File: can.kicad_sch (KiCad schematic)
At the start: 43 parts, among them Q3 2N7002, U5 TJA1051T/3, U6 MCP2518FD, U7 TJA1051T/3, Y1 40MHz

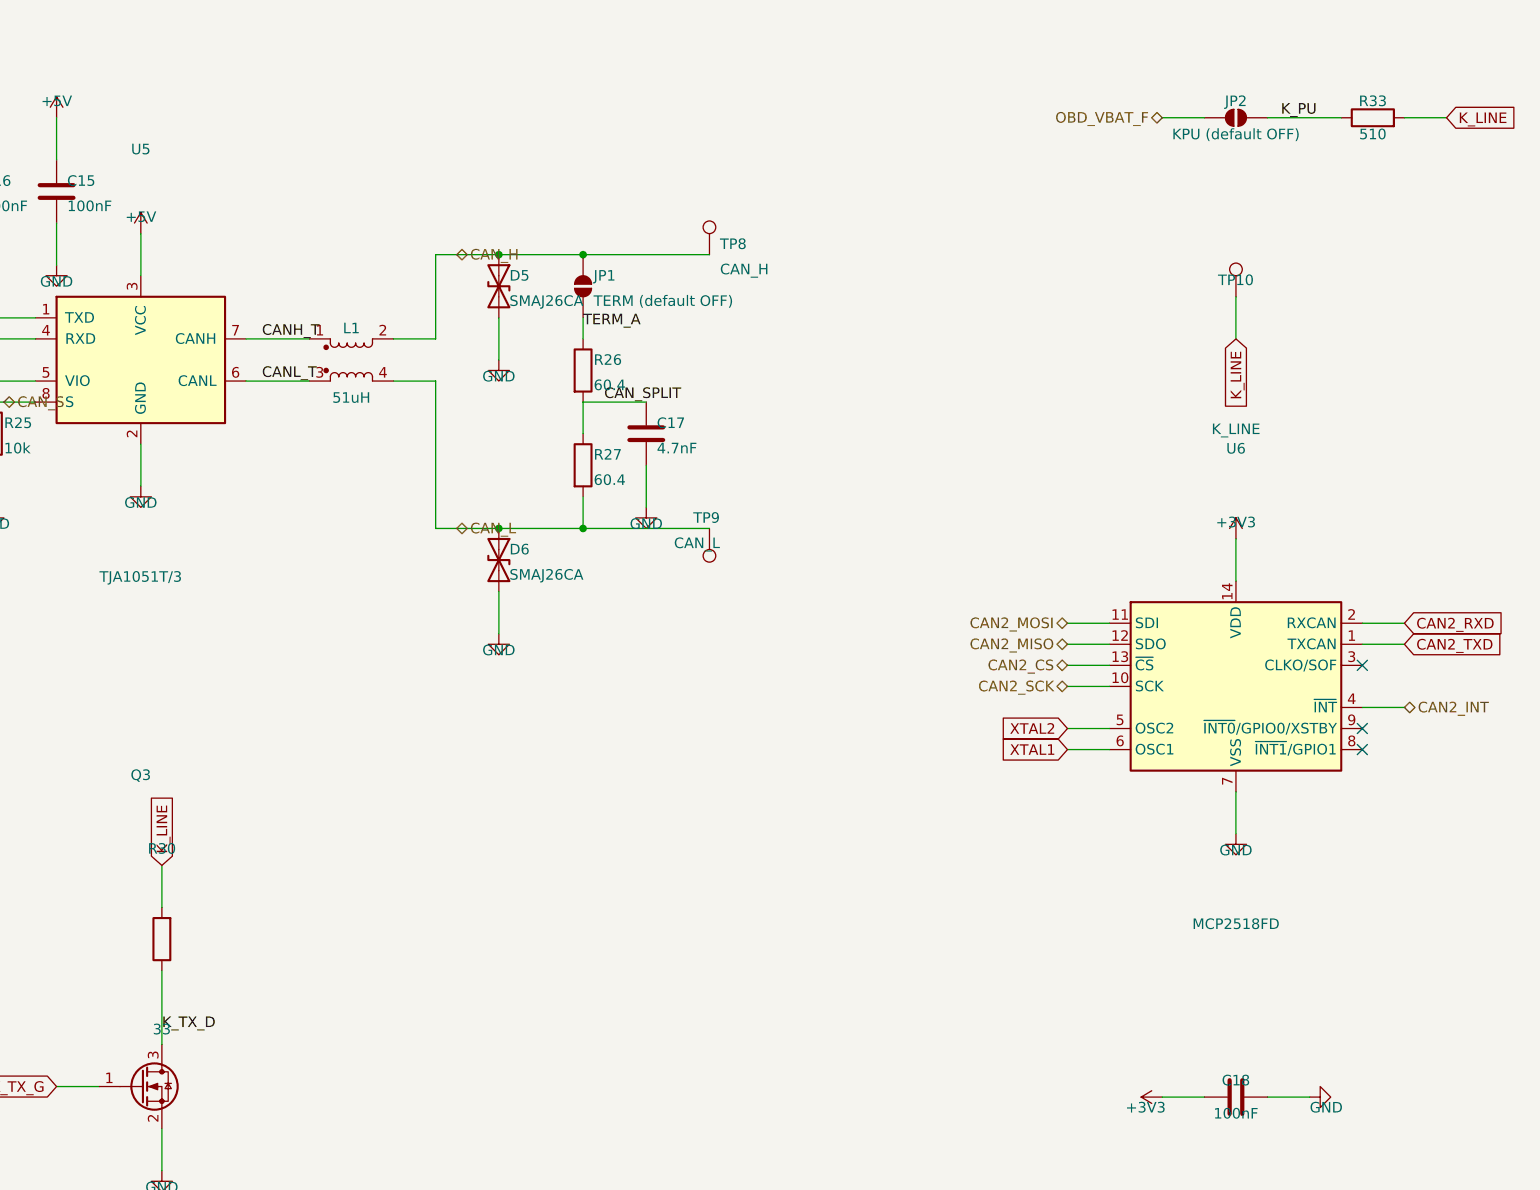
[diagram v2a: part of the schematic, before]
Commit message: Route, audit and document the carrier; verify every part number against the catalogue
Ordering is the point of this pass, so the part numbers came first. Every
LCSC number on the board was opened and read -- manufacturer part, package,
and the parameter that decides whether it is the right part. That found:

  C2148396 for the MCP2518FD    is an 18.7k resistor, out of stock -> C626759
  C255909  for a 40 MHz crystal is a 16 MHz crystal              -> C5186937
  C157966  for a JST PH 10-way  is a JST XH 9-way, 2.5 mm pitch  -> C158038

Three of the five numbers introduced last sitting were wrong, and all three
were plausible enough that the BOM exported clean. docs/PARTS.md records the
lot, including that LCSC's own listing for the microSD socket claims it has
no card-detect switch -- it has one, and the schematic is right.

Two footprints would not have soldered: both polyfuses are 1812 parts sitting
on a 1206 land, inherited from the parent board where nothing had ever
compared a part's package against its footprint. And the generic-passive
table was keyed on value alone, so the 1206 positions added last sitting
would have ordered 0805 parts -- right resistance, wrong footprint, every
board. It is keyed on (value, package) now and returns nothing rather than
guessing, so an unmatched line has no part number and somebody has to look.

Several values moved to match what is actually stocked: the power-fail
divider to 43k/18k (same trip point to 2 mV, both stocked 1 % parts), the
K-line series and pull-up to 20 R and 750 R, and the supercap charge resistor
from 22 R to 100 R -- 22 R put 1 W into a 250 mW part for the first several
seconds of every power-up.

Two real defects, both found by tools rather than by reading:

  - The hold-up Schottky was BACKWARDS. Reversed it shorts out the inrush
    limiter and blocks the discharge, so the supercap bank could never hold
    the rail up and the whole hold-up circuit was inert. audit_polarity found
    it once its expectat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
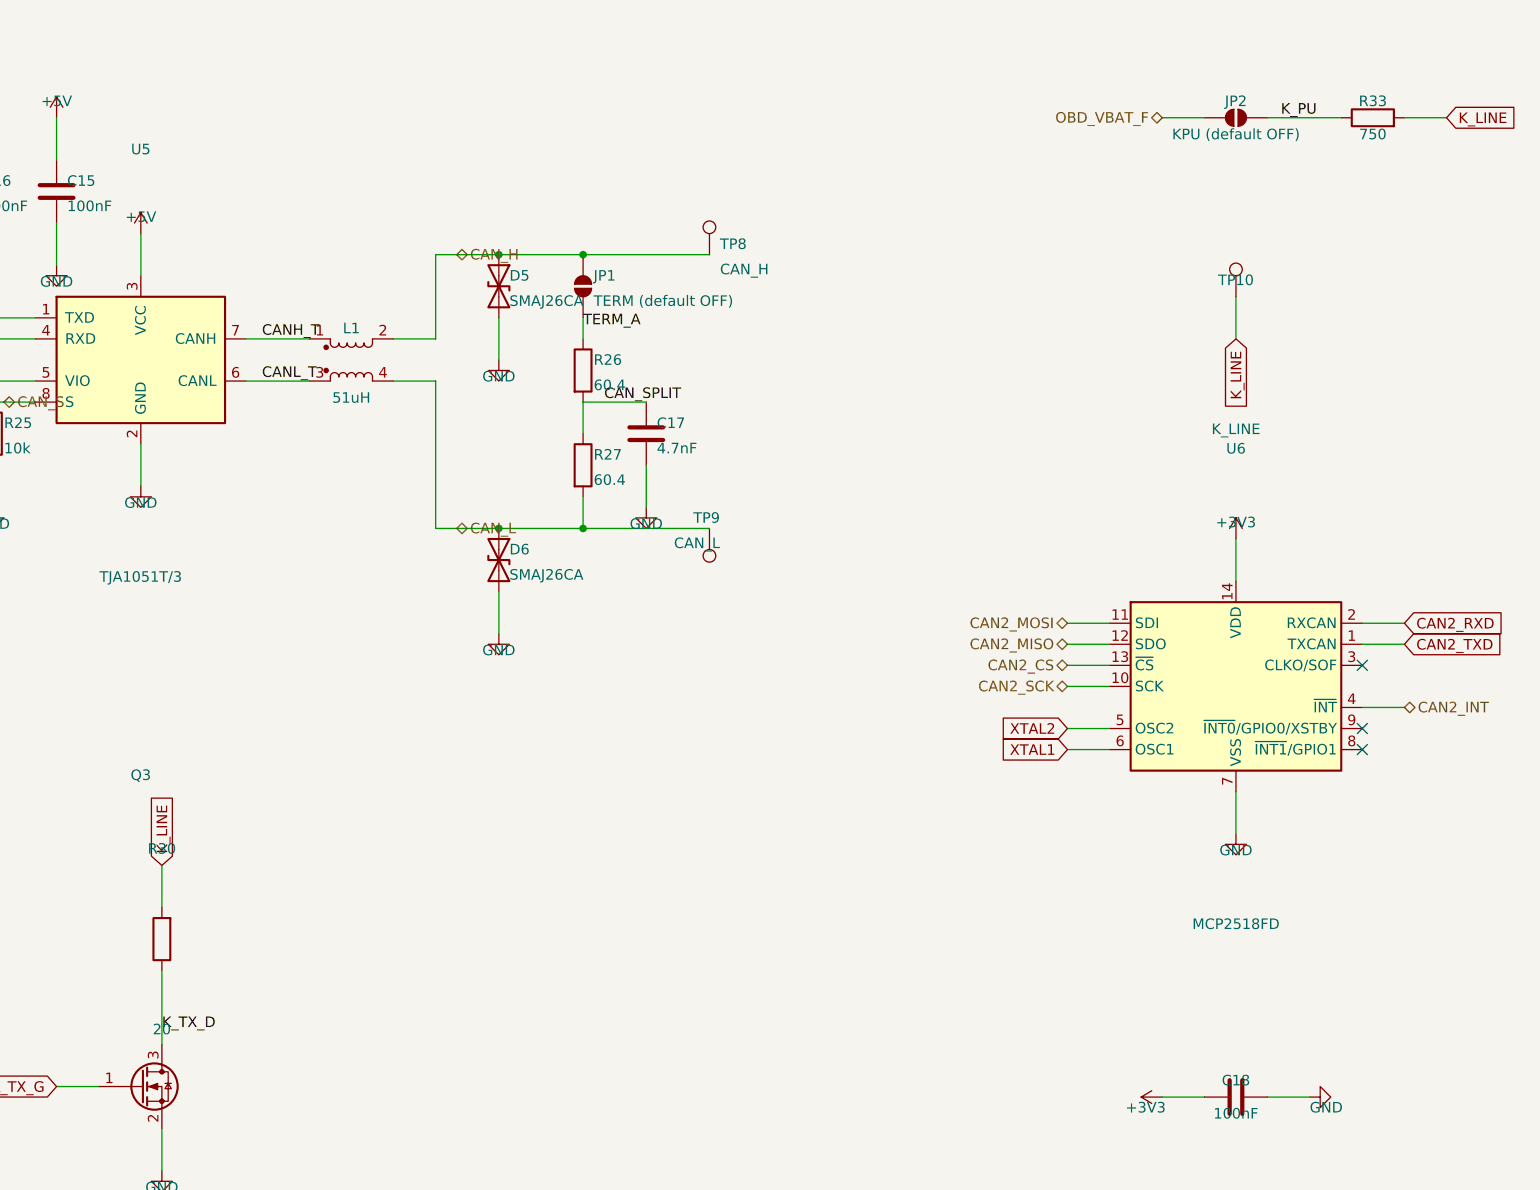
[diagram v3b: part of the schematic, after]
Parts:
- C20: Note Crystal load cap. Value assumes a crystal specified for 8 p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 -> Crystal load cap, sized for Y1's 12 pF CL: C1=C2=2*(CL - Cs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
- R30: value 33 -> 20; Note Series limit. ISO 9141-2 wants the tester's dominant below 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 -> Series limit, and the value is set by the worst of the two 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
- R33: value 510 -> 750; Note The ISO 9141-2 tester pull-up value. 1206: 12 V across it w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 -> The tester pull-up. ISO 9141-2 names 510 ohm; 750 is what e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
- Y1: MPN 40MHz 10ppm 3225 -> TX322540M4FBCE2T; Note 40 MHz, the top of the three rates the part accepts (4/20/40). Classic 500 kbit/s would be happy on 20, but 40 is what CAN FD data rates need and the crystals cost the same -> 40 MHz, the top of the three rates the part accepts (4/20/40). Classic 500 kbit/s would be happy on 20, but 40 is what CAN FD data rates need and the crystals cost the same. This one is -40/+85 C and 12 pF CL; the first part picked was -20/+70, which a car cabin exceeds in a summer car park
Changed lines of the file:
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@@
       (effects (font (size 1.27 1.27)) )
     )
-    (property "Value" "33" (at 49.53 127.73 0)
+    (property "Value" "20" (at 49.53 127.73 0)
       (effects (font (size 1.27 1.27)) )
     )
@@
       (effects (font (size 1.27 1.27)) hide)
     )
-    (property "Note" "Series limit. ISO 9141-2 wants the tester's dominant below 0.2*Vb: against the ECU's 510 ohm alone that is 12*33/543 = 0.73 V, and with the optional pull-up below also stuffed it is 1.38 V, both inside 2.4 V. Sized down from 100 ohm for exactly that second case. A sustained short of K-line to battery while transmitting puts 364 mA through the FET, over its 115 mA continuous rating -- it survives the pulse, not the fault. 1206 for the same reason" (at 49.53 127.73 0)
+    (property "Note" "Series limit, and the value is set by the worst of the two pull-up cases. ISO 9141-2 wants the tester's dominant below 0.2*Vb = 2.4 V. Including the FET's roughly 18 ohm Rds(on) at a 3.3 V gate the leg is about 38 ohm, so against the ECU's 510 ohm alone the dominant is 12*38/548 = 0.83 V, and with the optional 750 ohm below also stuffed (304 ohm combined) it is 1.33 V. Both clear. 33 ohm would also have worked and 100 ohm would not, but 20 is what exists in 1206. A sustained short of K-line to battery while transmitting puts about 316 mA through the FET, over its 115 mA continuous rating -- it survives the pulse, not the fault. 1206 carries the pulse energy" (at 49.53 127.73 0)
       (effects (font (size 1.27 1.27)) hide)
     )
@@
       (effects (font (size 1.27 1.27)) )
     )
-    (property "Value" "510" (at 195.58 19.78 270)
+    (property "Value" "750" (at 195.58 19.78 270)
       (effects (font (size 1.27 1.27)) )
     )
@@
       (effects (font (size 1.27 1.27)) hide)
     )
-    (property "Note" "The ISO 9141-2 tester pull-up value. 1206: 12 V across it while the line is dominant is 280 mW" (at 195.58 19.78 270)
+    (property "Note" "The tester pull-up. ISO 9141-2 names 510 ohm; 750 is what exists in 1206 and it is the better number here anyway -- the value is not critical, the ECU provides the real pull-up, and 750 dissipates 12^2/750 = 190 mW while the line is dominant against 510's 280 mW, which a 1206 rated 250 mW could not have carried" (at 195.58 19.78 270)
       (effects (font (size 1.27 1.27)) hide)
     )
@@
       (effects (font (size 1.27 1.27)) hide)
     )
-    (property "MPN" "40MHz 10ppm 3225" (at 179.07 210.28 0)
-      (effects (font (size 1.27 1.27)) hide)
-    )
-    (property "Note" "40 MHz, the top of the three rates the part accepts (4/20/40). Classic 500 kbit/s would be happy on 20, but 40 is what CAN FD data rates need and the crystals cost the same" (at 179.07 210.28 0)
+    (property "MPN" "TX322540M4FBCE2T" (at 179.07 210.28 0)
+      (effects (font (size 1.27 1.27)) hide)
+    )
+    (property "Note" "40 MHz, the top of the three rates the part accepts (4/20/40). Classic 500 kbit/s would be happy on 20, but 40 is what CAN FD data rates need and the crystals cost the same. This one is -40/+85 C and 12 pF CL; the first part picked was -20/+70, which a car cabin exceeds in a summer car park" (at 179.07 210.28 0)
       (effects (font (size 1.27 1.27)) hide)
     )
@@
       (effects (font (size 1.27 1.27)) hide)
     )
-    (property "Note" "Crystal load cap. Value assumes a crystal specified for 8 pF CL and about 5 pF of stray -- check CL on the part actually bought, an oscillator that starts on the bench and not at -20 C is the classic way to get this wrong" (at 179.07 233.14 270)
-      (effects (font (size 1.27 1.27)) hide)
-    )
+    (property "Note" "Crystal load cap, sized for Y1's 12 pF CL: C1=C2=2*(CL - Cstray) = 2*(12 - 5) = 14 pF, and 15 pF is the nearest E-series value. Re-check this if the crystal is substituted -- CL varies part to part, and an oscillator that starts on the bench but not at -20 C is the classic way to get it wrong" (at 179.07 233.14 270)
+      (effects (font (size 1.27 1.27)) hide)
+    )
